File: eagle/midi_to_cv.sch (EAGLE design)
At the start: 46 parts, among them IC2 4504N, IC3 4099N, U1 ATMEGA328P_PDIP

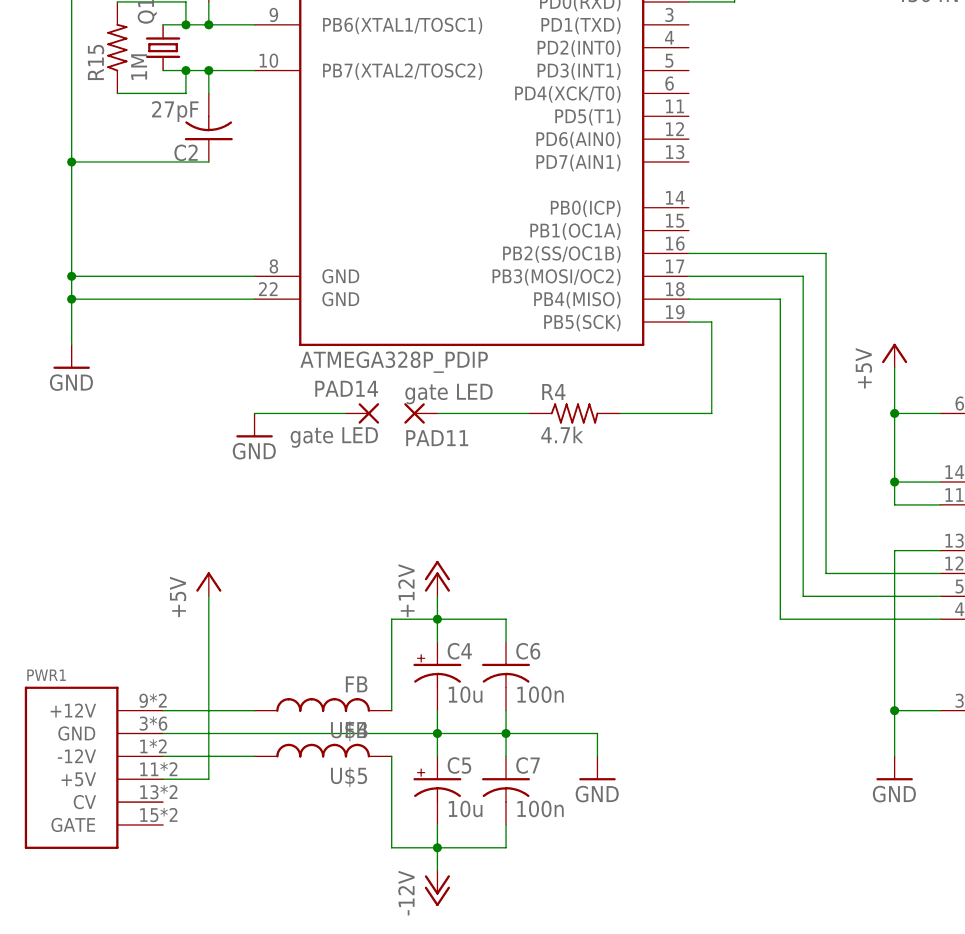
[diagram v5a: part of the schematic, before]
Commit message: 96 percent autorouting
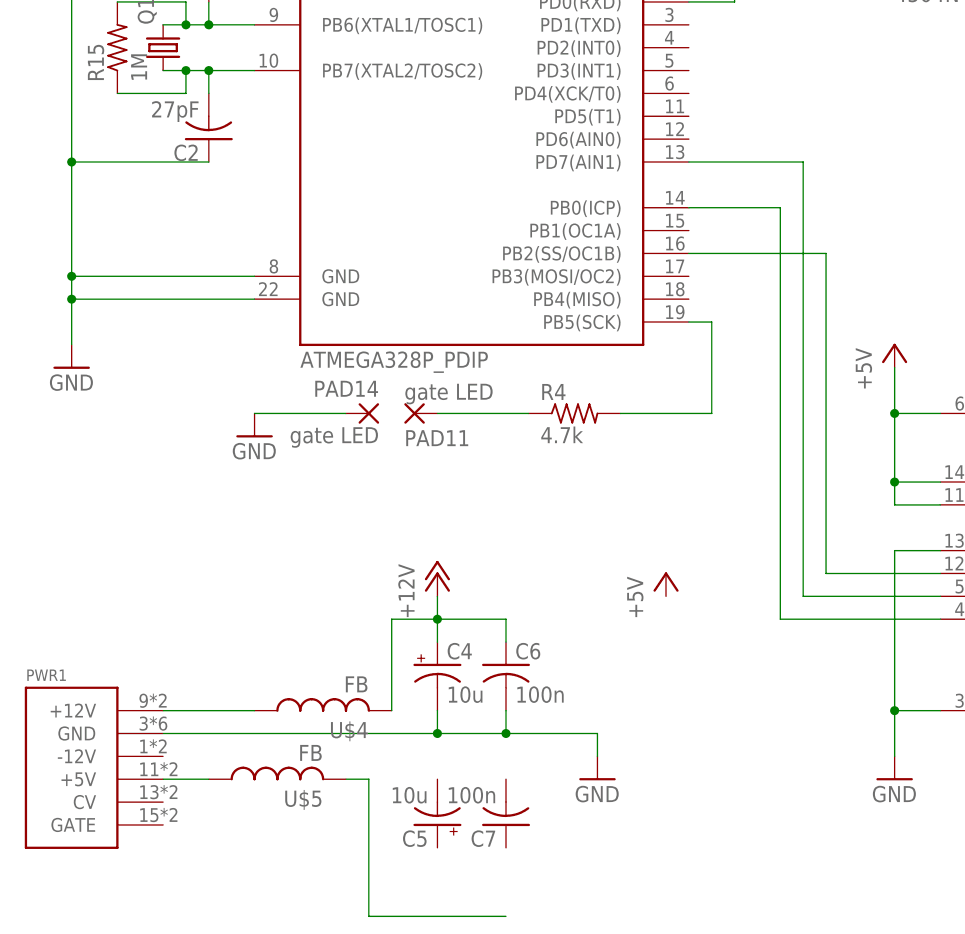
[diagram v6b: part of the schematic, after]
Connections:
- removed net -12V: C5.-, C7.2, U$5.2
- new net N$62: PWR1.+5V, U$5.1
- net +5V: no longer PWR1.+5V
- net N$13: now also U$5.2; no longer PWR1.-12V, U$5.1
- net N$14: now also U1.PD7(AIN1); no longer U1.PB3(MOSI/OC2)
- net N$26: no longer C5.+, C7.1
- net N$27: now also U1.PB0(ICP); no longer U1.PB4(MISO)
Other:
- moved on the sheet: C5, C7, U$5
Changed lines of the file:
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@@
 <part name="C5" library="rcl" deviceset="CPOL-US" device="B45181A" value="10u"/>
 <part name="P+14" library="supply1" deviceset="+12V" device=""/>
-<part name="P-4" library="supply1" deviceset="-12V" device=""/>
 <part name="GND13" library="supply1" deviceset="GND" device=""/>
 <part name="C6" library="rcl" deviceset="C-US" device="050-024X044" value="100n"/>
@@
 <instance part="P+1" gate="1" x="-20.32" y="91.44"/>
 <instance part="GND1" gate="1" x="-25.4" y="10.16"/>
-<instance part="P+3" gate="1" x="-10.16" y="-12.7"/>
+<instance part="P+3" gate="1" x="40.64" y="-12.7"/>
 <instance part="PAD11" gate="1" x="12.7" y="5.08" rot="MR180"/>
 <instance part="R4" gate="G$1" x="30.48" y="5.08"/>
@@
 <instance part="PWR1" gate="G$1" x="-25.4" y="-33.02"/>
 <instance part="U$4" gate="G$1" x="2.54" y="-27.94" rot="R90"/>
-<instance part="U$5" gate="G$1" x="2.54" y="-33.02" rot="R90"/>
+<instance part="U$5" gate="G$1" x="-2.54" y="-35.56" rot="R90"/>
 <instance part="C4" gate="G$1" x="15.24" y="-22.86"/>
-<instance part="C5" gate="G$1" x="15.24" y="-35.56"/>
+<instance part="C5" gate="G$1" x="15.24" y="-40.64" rot="R180"/>
 <instance part="P+14" gate="1" x="15.24" y="-12.7"/>
-<instance part="P-4" gate="1" x="15.24" y="-48.26"/>
 <instance part="GND13" gate="1" x="33.02" y="-35.56"/>
 <instance part="C6" gate="G$1" x="22.86" y="-22.86"/>
-<instance part="C7" gate="G$1" x="22.86" y="-35.56"/>
+<instance part="C7" gate="G$1" x="22.86" y="-40.64" rot="R180"/>
 <instance part="R15" gate="G$1" x="-20.32" y="45.72" rot="R90"/>
 <instance part="IC2" gate="A" x="73.66" y="66.04"/>
@@
 </segment>
 <segment>
-<pinref part="PWR1" gate="G$1" pin="+5V"/>
-<pinref part="P+3" gate="1" pin="+5V"/>
-<wire x1="-15.24" y1="-35.56" x2="-10.16" y2="-35.56" width="0.1524" layer="91"/>
-<wire x1="-10.16" y1="-35.56" x2="-10.16" y2="-15.24" width="0.1524" layer="91"/>
-</segment>
-<segment>
 <pinref part="IC2" gate="P" pin="VCC"/>
 <pinref part="P+4" gate="1" pin="+5V"/>
@@
 </segment>
 </net>
-<net name="-12V" class="0">
-<segment>
-<pinref part="C5" gate="G$1" pin="-"/>
-<pinref part="P-4" gate="1" pin="-12V"/>
-<wire x1="15.24" y1="-45.72" x2="15.24" y2="-43.18" width="0.1524" layer="91"/>
-<pinref part="U$5" gate="G$1" pin="2"/>
-<wire x1="15.24" y1="-43.18" x2="15.24" y2="-40.64" width="0.1524" layer="91"/>
-<wire x1="10.16" y1="-33.02" x2="10.16" y2="-43.18" width="0.1524" layer="91"/>
-<wire x1="10.16" y1="-43.18" x2="15.24" y2="-43.18" width="0.1524" layer="91"/>
-<junction x="15.24" y="-43.18"/>
-<pinref part="C7" gate="G$1" pin="2"/>
-<wire x1="22.86" y1="-40.64" x2="22.86" y2="-43.18" width="0.1524" layer="91"/>
-<wire x1="22.86" y1="-43.18" x2="15.24" y2="-43.18" width="0.1524" layer="91"/>
-</segment>
-</net>
 <net name="N$27" class="0">
 <segment>
-<pinref part="U1" gate="G$1" pin="PB4(MISO)"/>
-<wire x1="43.18" y1="17.78" x2="53.34" y2="17.78" width="0.1524" layer="91"/>
-<wire x1="53.34" y1="17.78" x2="53.34" y2="-17.78" width="0.1524" layer="91"/>
+<wire x1="53.34" y1="27.94" x2="53.34" y2="-17.78" width="0.1524" layer="91"/>
 <pinref part="U$11" gate="G$1" pin="DATA"/>
 <wire x1="53.34" y1="-17.78" x2="71.12" y2="-17.78" width="0.1524" layer="91"/>
+<pinref part="U1" gate="G$1" pin="PB0(ICP)"/>
+<wire x1="43.18" y1="27.94" x2="53.34" y2="27.94" width="0.1524" layer="91"/>
 </segment>
 </net>
@@
 <net name="N$14" class="0">
 <segment>
-<pinref part="U1" gate="G$1" pin="PB3(MOSI/OC2)"/>
-<wire x1="43.18" y1="20.32" x2="55.88" y2="20.32" width="0.1524" layer="91"/>
-<wire x1="55.88" y1="20.32" x2="55.88" y2="-15.24" width="0.1524" layer="91"/>
+<wire x1="55.88" y1="33.02" x2="55.88" y2="-15.24" width="0.1524" layer="91"/>
 <pinref part="U$11" gate="G$1" pin="CLK"/>
 <wire x1="55.88" y1="-15.24" x2="71.12" y2="-15.24" width="0.1524" layer="91"/>
+<pinref part="U1" gate="G$1" pin="PD7(AIN1)"/>
+<wire x1="55.88" y1="33.02" x2="43.18" y2="33.02" width="0.1524" layer="91"/>
 </segment>
 </net>
@@
 <wire x1="15.24" y1="-27.94" x2="15.24" y2="-30.48" width="0.1524" layer="91"/>
 <junction x="15.24" y="-30.48"/>
-<pinref part="C5" gate="G$1" pin="+"/>
-<wire x1="15.24" y1="-33.02" x2="15.24" y2="-30.48" width="0.1524" layer="91"/>
 <pinref part="C6" gate="G$1" pin="2"/>
 <wire x1="22.86" y1="-27.94" x2="22.86" y2="-30.48" width="0.1524" layer="91"/>
 <junction x="22.86" y="-30.48"/>
-<pinref part="C7" gate="G$1" pin="1"/>
-<wire x1="22.86" y1="-33.02" x2="22.86" y2="-30.48" width="0.1524" layer="91"/>
 </segment>
 </net>
@@
 <pinref part="U$4" gate="G$1" pin="1"/>
 <wire x1="-15.24" y1="-27.94" x2="-5.08" y2="-27.94" width="0.1524" layer="91"/>
-</segment>
-</net>
-<net name="N$13" class="0">
-<segment>
-<pinref part="PWR1" gate="G$1" pin="-12V"/>
-<pinref part="U$5" gate="G$1" pin="1"/>
-<wire x1="-15.24" y1="-33.02" x2="-5.08" y2="-33.02" width="0.1524" layer="91"/>
 </segment>
 </net>
@@
 </segment>
 </net>
+<net name="N$62" class="0">
+<segment>
+<pinref part="PWR1" gate="G$1" pin="+5V"/>
+<wire x1="-15.24" y1="-35.56" x2="-10.16" y2="-35.56" width="0.1524" layer="91"/>
+<pinref part="U$5" gate="G$1" pin="1"/>
+</segment>
+</net>
+<net name="N$13" class="0">
+<segment>
+<pinref part="U$5" gate="G$1" pin="2"/>
+<wire x1="5.08" y1="-35.56" x2="7.62" y2="-35.56" width="0.1524" layer="91"/>
+<wire x1="7.62" y1="-35.56" x2="7.62" y2="-50.8" width="0.1524" layer="91"/>
+<wire x1="22.86" y1="-50.8" x2="7.62" y2="-50.8" width="0.1524" layer="91"/>
+</segment>
+</net>

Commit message: routed
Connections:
- removed net N$13: U$5.2
- net +5V: now also C5.+, C7.1, U$5.2
- net N$26: now also C5.-, C7.2
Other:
- moved on the sheet: U$4
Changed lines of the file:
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@@
 <instance part="GND11" gate="1" x="-5.08" y="2.54"/>
 <instance part="PWR1" gate="G$1" x="-25.4" y="-33.02"/>
-<instance part="U$4" gate="G$1" x="2.54" y="-27.94" rot="R90"/>
+<instance part="U$4" gate="G$1" x="-2.54" y="-27.94" rot="R90"/>
 <instance part="U$5" gate="G$1" x="-2.54" y="-35.56" rot="R90"/>
 <instance part="C4" gate="G$1" x="15.24" y="-22.86"/>
@@
 <junction x="66.04" y="5.08"/>
 </segment>
+<segment>
+<pinref part="U$5" gate="G$1" pin="2"/>
+<wire x1="5.08" y1="-35.56" x2="5.08" y2="-50.8" width="0.1524" layer="91"/>
+<pinref part="P+3" gate="1" pin="+5V"/>
+<wire x1="5.08" y1="-50.8" x2="15.24" y2="-50.8" width="0.1524" layer="91"/>
+<wire x1="15.24" y1="-50.8" x2="22.86" y2="-50.8" width="0.1524" layer="91"/>
+<wire x1="22.86" y1="-50.8" x2="40.64" y2="-50.8" width="0.1524" layer="91"/>
+<wire x1="40.64" y1="-50.8" x2="40.64" y2="-15.24" width="0.1524" layer="91"/>
+<pinref part="C5" gate="G$1" pin="+"/>
+<wire x1="15.24" y1="-43.18" x2="15.24" y2="-50.8" width="0.1524" layer="91"/>
+<junction x="15.24" y="-50.8"/>
+<pinref part="C7" gate="G$1" pin="1"/>
+<wire x1="22.86" y1="-43.18" x2="22.86" y2="-50.8" width="0.1524" layer="91"/>
+<junction x="22.86" y="-50.8"/>
+</segment>
 </net>
 <net name="GND" class="0">
@@
 <pinref part="U$4" gate="G$1" pin="2"/>
 <wire x1="15.24" y1="-17.78" x2="15.24" y2="-20.32" width="0.1524" layer="91"/>
-<wire x1="10.16" y1="-27.94" x2="10.16" y2="-17.78" width="0.1524" layer="91"/>
-<wire x1="10.16" y1="-17.78" x2="15.24" y2="-17.78" width="0.1524" layer="91"/>
+<wire x1="5.08" y1="-27.94" x2="5.08" y2="-17.78" width="0.1524" layer="91"/>
+<wire x1="5.08" y1="-17.78" x2="15.24" y2="-17.78" width="0.1524" layer="91"/>
 <junction x="15.24" y="-17.78"/>
 <pinref part="C6" gate="G$1" pin="1"/>
@@
 <wire x1="22.86" y1="-27.94" x2="22.86" y2="-30.48" width="0.1524" layer="91"/>
 <junction x="22.86" y="-30.48"/>
+<pinref part="C7" gate="G$1" pin="2"/>
+<wire x1="22.86" y1="-35.56" x2="22.86" y2="-30.48" width="0.1524" layer="91"/>
+<pinref part="C5" gate="G$1" pin="-"/>
+<wire x1="15.24" y1="-35.56" x2="15.24" y2="-30.48" width="0.1524" layer="91"/>
 </segment>
 </net>
@@
 <pinref part="PWR1" gate="G$1" pin="+12V"/>
 <pinref part="U$4" gate="G$1" pin="1"/>
-<wire x1="-15.24" y1="-27.94" x2="-5.08" y2="-27.94" width="0.1524" layer="91"/>
+<wire x1="-15.24" y1="-27.94" x2="-10.16" y2="-27.94" width="0.1524" layer="91"/>
 </segment>
 </net>
@@
 </segment>
 </net>
-<net name="N$13" class="0">
-<segment>
-<pinref part="U$5" gate="G$1" pin="2"/>
-<wire x1="5.08" y1="-35.56" x2="7.62" y2="-35.56" width="0.1524" layer="91"/>
-<wire x1="7.62" y1="-35.56" x2="7.62" y2="-50.8" width="0.1524" layer="91"/>
-<wire x1="22.86" y1="-50.8" x2="7.62" y2="-50.8" width="0.1524" layer="91"/>
-</segment>
-</net>

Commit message: mid nineties autoroute
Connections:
- net N$33: now also IC2A.CO; no longer IC2A.AO
- net N$36: now also IC2A.AO; no longer IC2A.CO
- net N$37: now also IC3A.D; no longer IC3A.!E
- net N$38: now also IC3A.!E; no longer IC3A.D
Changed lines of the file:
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@@
-</segment>
-</net>
-<net name="N$33" class="0">
-<segment>
-<pinref part="IC2" gate="A" pin="AO"/>
-<pinref part="IC3" gate="A" pin="A0"/>
-<wire x1="86.36" y1="73.66" x2="99.06" y2="73.66" width="0.1524" layer="91"/>
-<wire x1="99.06" y1="73.66" x2="99.06" y2="45.72" width="0.1524" layer="91"/>
 </segment>
 </net>
 <net name="N$35" class="0">
 <segment>
+<pinref part="IC3" gate="A" pin="A1"/>
+<wire x1="96.52" y1="43.18" x2="99.06" y2="43.18" width="0.1524" layer="91"/>
 <pinref part="IC2" gate="A" pin="BO"/>
-<pinref part="IC3" gate="A" pin="A1"/>
 <wire x1="86.36" y1="71.12" x2="96.52" y2="71.12" width="0.1524" layer="91"/>
 <wire x1="96.52" y1="71.12" x2="96.52" y2="43.18" width="0.1524" layer="91"/>
-<wire x1="96.52" y1="43.18" x2="99.06" y2="43.18" width="0.1524" layer="91"/>
 </segment>
 </net>
 <net name="N$36" class="0">
 <segment>
-<pinref part="IC2" gate="A" pin="CO"/>
 <pinref part="IC3" gate="A" pin="A2"/>
-<wire x1="86.36" y1="68.58" x2="93.98" y2="68.58" width="0.1524" layer="91"/>
-<wire x1="93.98" y1="68.58" x2="93.98" y2="40.64" width="0.1524" layer="91"/>
 <wire x1="93.98" y1="40.64" x2="99.06" y2="40.64" width="0.1524" layer="91"/>
+<wire x1="93.98" y1="40.64" x2="93.98" y2="73.66" width="0.1524" layer="91"/>
+<pinref part="IC2" gate="A" pin="AO"/>
+<wire x1="93.98" y1="73.66" x2="86.36" y2="73.66" width="0.1524" layer="91"/>
 </segment>
 </net>
@@
 <pinref part="IC2" gate="A" pin="DO"/>
 <wire x1="86.36" y1="66.04" x2="91.44" y2="66.04" width="0.1524" layer="91"/>
-<wire x1="91.44" y1="66.04" x2="91.44" y2="33.02" width="0.1524" layer="91"/>
-<pinref part="IC3" gate="A" pin="!E"/>
-<wire x1="91.44" y1="33.02" x2="99.06" y2="33.02" width="0.1524" layer="91"/>
+<wire x1="91.44" y1="66.04" x2="91.44" y2="30.48" width="0.1524" layer="91"/>
+<pinref part="IC3" gate="A" pin="D"/>
+<wire x1="91.44" y1="30.48" x2="99.06" y2="30.48" width="0.1524" layer="91"/>
 </segment>
 </net>
@@
 <pinref part="IC2" gate="A" pin="EO"/>
 <wire x1="86.36" y1="63.5" x2="88.9" y2="63.5" width="0.1524" layer="91"/>
-<wire x1="88.9" y1="63.5" x2="88.9" y2="30.48" width="0.1524" layer="91"/>
-<pinref part="IC3" gate="A" pin="D"/>
-<wire x1="88.9" y1="30.48" x2="99.06" y2="30.48" width="0.1524" layer="91"/>
+<wire x1="88.9" y1="63.5" x2="88.9" y2="33.02" width="0.1524" layer="91"/>
+<pinref part="IC3" gate="A" pin="!E"/>
+<wire x1="99.06" y1="33.02" x2="88.9" y2="33.02" width="0.1524" layer="91"/>
 </segment>
 </net>
@@
 </segment>
 </net>
-<net name="N$23" class="0">
+<net name="N$62" class="0">
+<segment>
+<pinref part="PWR1" gate="G$1" pin="+5V"/>
+<wire x1="-15.24" y1="-35.56" x2="-10.16" y2="-35.56" width="0.1524" layer="91"/>
+<pinref part="U$5" gate="G$1" pin="1"/>
+</segment>
+</net>
+<net name="N$13" class="0">
 <segment>
 <pinref part="U1" gate="G$1" pin="PC0(ADC0)"/>
@@
 </segment>
 </net>
-<net name="N$25" class="0">
+<net name="N$23" class="0">
 <segment>
 <pinref part="IC2" gate="A" pin="BI"/>
@@
 </segment>
 </net>
-<net name="N$30" class="0">
+<net name="N$25" class="0">
 <segment>
 <pinref part="U1" gate="G$1" pin="PC2(ADC2)"/>
@@
 </segment>
 </net>
+<net name="N$30" class="0">
+<segment>
+<pinref part="IC2" gate="A" pin="DI"/>
+<pinref part="U1" gate="G$1" pin="PC5(ADC5/SCL)"/>
+<wire x1="60.96" y1="66.04" x2="43.18" y2="60.96" width="0.1524" layer="91"/>
+</segment>
+</net>
 <net name="N$31" class="0">
 <segment>
@@
 </segment>
 </net>
-<net name="N$34" class="0">
-<segment>
-<pinref part="U1" gate="G$1" pin="PC5(ADC5/SCL)"/>
-<pinref part="IC2" gate="A" pin="DI"/>
-<wire x1="43.18" y1="60.96" x2="60.96" y2="66.04" width="0.1524" layer="91"/>
-</segment>
-</net>
-<net name="N$62" class="0">
-<segment>
-<pinref part="PWR1" gate="G$1" pin="+5V"/>
-<wire x1="-15.24" y1="-35.56" x2="-10.16" y2="-35.56" width="0.1524" layer="91"/>
-<pinref part="U$5" gate="G$1" pin="1"/>
-</segment>
-</net>
+<net name="N$33" class="0">
+<segment>
+<pinref part="IC3" gate="A" pin="A0"/>
+<wire x1="99.06" y1="45.72" x2="99.06" y2="68.58" width="0.1524" layer="91"/>
+<pinref part="IC2" gate="A" pin="CO"/>
+<wire x1="99.06" y1="68.58" x2="86.36" y2="68.58" width="0.1524" layer="91"/>
+</segment>
+</net>
